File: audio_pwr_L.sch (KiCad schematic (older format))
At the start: 43 parts, among them Q201 BC546, Q202 BC546, Q203 BC546, Q204 BD140, Q205 BD139, Q206 BD140, Q207 MJL21193, Q208 MJL21194, Q209 BC546

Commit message: Lots of part changes to SMD devices. Adding MPN, MFG to all parts for BOM export.
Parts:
- removed F201, F202: 3A, Fuseholders:Fuseholder5x20_horiz_open_inline_Type-I, symbol Device:Fuse
- removed Q201, Q202: BC546, Package_TO_SOT_THT:TO-92_Inline, symbol AAMB-rescue:BC546-transistors
- added F201, F202: 0154003.DR, Fuse:0154003.DR, symbol Fuse:0154003.DR
- added TP7: 5002, digikey-footprints:Test_Point_D1.02mm, symbol dk_Test-Points:5002
- added TP8: 5000, digikey-footprints:Test_Point_D1.02mm, symbol dk_Test-Points:5000
- added TP9: 5001, digikey-footprints:Test_Point_D1.02mm, symbol dk_Test-Points:5001
- added U201: BC846BDW1T1G, Package_TO_SOT_SMD:SOT-363_SC-70-6, symbol OnSemi_BC846:BC846BDW1T1G
- C201: footprint Capacitor_THT:CP_Radial_D5.0mm_P2.00mm -> Capacitor_SMD:CP_Elec_4x5.4; DigiKey (none) -> https://www.we-online.de/katalog/datasheet/865080640004.pdf; MFG (none) -> Würth Elektronik; MPN (none) -> 865080640004
- C202, C204, C206: footprint Capacitor_THT:C_Disc_D5.1mm_W3.2mm_P5.00mm -> Capacitor_SMD:C_0603_1608Metric_Pad1.05x0.95mm_HandSolder; DigiKey (none) -> https://www.digikey.com/product-detail/en/w%C3%BCrth-elektr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; MFG (none) -> Würth Elektronik; MPN (none) -> 885012006057
- C203: footprint Capacitor_THT:CP_Radial_D10.0mm_P5.00mm -> Capacitor_SMD:C_Elec_5x5.4; DigiKey (none) -> https://www.digikey.com/product-detail/en/w%C3%BCrth-elektr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; MFG (none) -> Würth Elektronik; MPN (none) -> 865080142007
- C205: footprint Capacitor_THT:CP_Radial_D10.0mm_P5.00mm -> Capacitor_SMD:C_Elec_6.3x7.7; DigiKey (none) -> https://www.digikey.com/product-detail/en/w%C3%BCrth-elektr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; MFG (none) -> Würth Elektronik; MPN (none) -> 865080545012
- C207, C208, C209: DigiKey (none) -> https://www.digikey.com/product-detail/en/kemet/R82EC3100AA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; MFG (none) -> KEMET; MPN (none) -> R82EC3100AA70K
- C210, C211: footprint Capacitor_THT:CP_Radial_D10.0mm_P5.00mm -> Capacitor_SMD:CP_Elec_10x10.5; DigiKey (none) -> https://www.digikey.com/product-detail/en/nichicon/UUX1J101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; MFG (none) -> Nichicon; MPN (none) -> UUX1J101MNL1GS
- D201: footprint LED_THT:LED_D3.0mm -> LED_SMD:LED_0603_1608Metric_Pad1.05x0.95mm_HandSolder; DigiKey (none) -> https://www.digikey.com/product-detail/en/rohm-semiconducto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; MFG (none) -> Rohm Semiconductor; MPN (none) -> SML-D12U1WT86
- Q203, Q209: value BC546 -> BC846; footprint Package_TO_SOT_THT:TO-92_Inline -> Package_TO_SOT_SMD:SOT-23; DigiKey (none) -> https://www.digikey.com/product-detail/en/on-semiconductor/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; MFG (none) -> ON Semiconductor; MPN (none) -> BC846BLT1G
- Q204, Q206: value BD140 -> BCP53; footprint Package_TO_SOT_THT:TO-126-3_Vertical -> Package_TO_SOT_SMD:SOT-223; DigiKey (none) -> https://www.digikey.com/product-detail/en/on-semiconductor/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; MFG (none) -> ON Semiconductor; MPN (none) -> SBCP53-10T1G
- Q205: value BD139 -> BCP56; footprint Package_TO_SOT_THT:TO-126-3_Vertical -> Package_TO_SOT_SMD:SOT-223; DigiKey (none) -> https://www.digikey.com/product-detail/en/on-semiconductor/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; MFG (none) -> ON Semiconductor; MPN (none) -> SBCP56-16T3G
- R213, R214: value 15m -> 330m; footprint Resistor_THT:R_Axial_Power_L25.0mm_W9.0mm_P10.16mm_Vertical -> Resistor_THT:R_Radial_Power_L13.0mm_W9.0mm_P5.00mm; DigiKey (none) -> https://www.digikey.com/product-detail/en/te-connectivity-p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; MFG (none) -> TE Connectivity Passive Product; MPN (none) -> SQMW5R33J
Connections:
- wire segments 123 -> 128

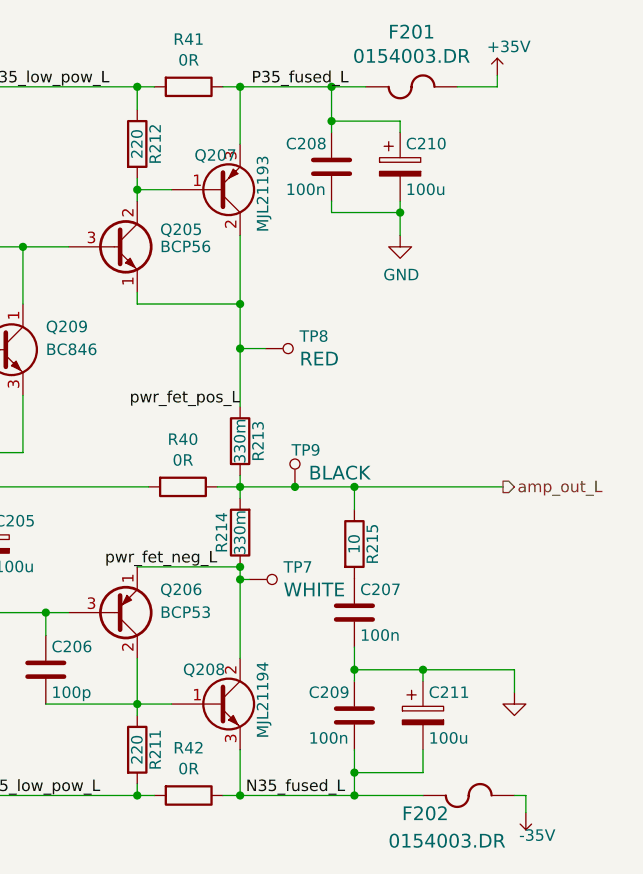
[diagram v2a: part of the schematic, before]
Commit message: Layout startover, sorting, some routing. Removed redundant fuses. BOM export.
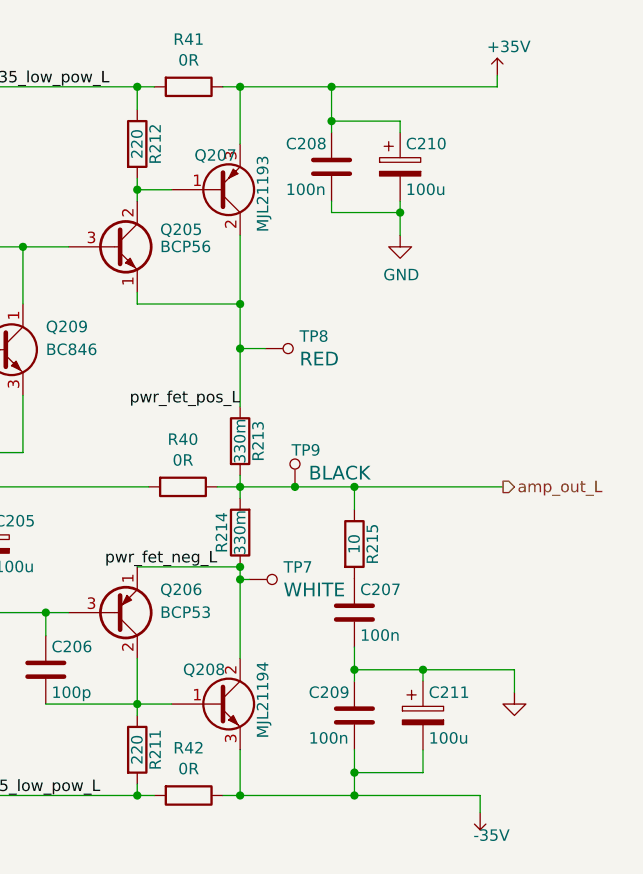
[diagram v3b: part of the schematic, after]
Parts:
- removed F201, F202: 0154003.DR, Fuse:0154003.DR, symbol Fuse:0154003.DR
- C201, C202, C203, C204, C205, C206: MFG Würth Elektronik -> Wurth Elektronik
- Q207: DigiKey (none) -> https://www.digikey.com/products/en/discrete-semiconductor-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; MFG (none) -> ON Semiconductor; MPN (none) -> MJL21193G
- Q208: DigiKey (none) -> https://www.digikey.com/products/en/discrete-semiconductor-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; MFG (none) -> ON Semiconductor; MPN (none) -> MJL21194G
- R201, R203, R204, R216: DigiKey (none) -> https://www.digikey.com/product-detail/en/vishay-dale/RCS06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; MFG (none) -> Vishay Dale; MPN (none) -> RCS06031K00FKEA
- R202, R205, R208: DigiKey (none) -> https://www.digikey.com/product-detail/en/te-connectivity-p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; MFG (none) -> TE Connectivity Passive Product; MPN (none) -> CRGCQ0603F22K
- R206, R207: DigiKey (none) -> https://www.digikey.com/product-detail/en/te-connectivity-p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; MFG (none) -> TE Connectivity Passive Product; MPN (none) -> CRGCQ0603F560R
- R209, R210: DigiKey (none) -> https://www.digikey.com/product-detail/en/vishay-dale/CRCW0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; MFG (none) -> Vishay Dale; MPN (none) -> CRCW06033K30FKEA
- R211, R212: DigiKey (none) -> https://www.digikey.com/product-detail/en/panasonic-electro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; MFG (none) -> Panasonic Electronic Components; MPN (none) -> ERJ-PA3F2200V
- R215: DigiKey (none) -> https://www.digikey.com/product-detail/en/panasonic-electro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; MFG (none) -> Panasonic Electronic Components; MPN (none) -> ERJ-PA3F10R0V
- R40, R41, R42: MFG (none) -> Stackpole Electronics Inc; MPN (none) -> RMCF1210ZT0R00
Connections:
- net N35_fused_L is gone; now on net -35V: C209.2, C211.2, Q208.3 (E), R42.1
- net P35_fused_L is gone; now on net +35V: C208.1, C210.1, Q207.3 (E), R41.1

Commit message: Capturing layout progress.
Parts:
- removed C201: 4.7u, Capacitor_SMD:CP_Elec_4x5.4, symbol Device:CP
- removed TP7: 5002, digikey-footprints:Test_Point_D1.02mm, symbol dk_Test-Points:5002
- removed TP8: 5000, digikey-footprints:Test_Point_D1.02mm, symbol dk_Test-Points:5000
- removed TP9: 5001, digikey-footprints:Test_Point_D1.02mm, symbol dk_Test-Points:5001
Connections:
- net amp_in_L: now also R201.2
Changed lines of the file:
@@
 Connection ~ 3300 4350
-Wire Wire Line
-	2900 3650 2950 3650
 Wire Wire Line
 	3850 4450 3850 4350
@@
 	6900 3600 6900 3650
 Connection ~ 6900 3650
-Wire Wire Line
-	6900 4000 6900 4055
 $Comp
 L Device:Q_PNP_BCE Q207
@@
 Wire Wire Line
 	6450 2350 6450 2400
-Wire Wire Line
-	6900 2850 6900 3045
 Connection ~ 3300 3800
 Text Label 6800 4000 2    50   ~ 0
@@
 Wire Wire Line
 	4900 4400 4900 4500
-Text HLabel 2450 3650 0    50   Input ~ 0
+Text HLabel 2700 3650 0    50   Input ~ 0
 amp_in_L
 Text HLabel 8050 3650 2    50   Output ~ 0
@@
 Wire Wire Line
 	7400 3650 8050 3650
-$Comp
-L Device:CP C201
-U 1 1 5C7F66CB
-P 2750 3650
-F 0 "C201" H 2775 3750 50  0000 L CNN
-F 1 "4.7u" H 2775 3550 50  0000 L CNN
-F 2 "Capacitor_SMD:CP_Elec_4x5.4" H 2788 3500 50  0001 C CNN
-F 3 "https://www.digikey.com/product-detail/en/w%C3%BCrth-elektronik/865080640004/732-8449-1-ND/5728406" H 2750 3650 50  0001 C CNN
-F 4 "https://www.we-online.de/katalog/datasheet/865080640004.pdf" H 2750 3650 50  0001 C CNN "DigiKey"
-F 5 "Wurth Elektronik" H 2750 3650 50  0001 C CNN "MFG"
-F 6 "865080640004" H 2750 3650 50  0001 C CNN "MPN"
-	1    2750 3650
-	0    -1   -1   0
-$EndComp
 $Comp
 L Device:R R203
@@
 	3000 4500 3000 4350
 Wire Wire Line
-	2450 3650 2600 3650
-Wire Wire Line
 	7600 2450 7600 2550
 $Comp
@@
 	7400 5000 6900 5000
 Connection ~ 7400 5000
-Wire Wire Line
-	7400 3650 7140 3650
 Connection ~ 7400 3650
 $Comp
@@
 Wire Wire Line
 	4700 3650 4900 3650
-$Comp
-L dk_Test-Points:5000 TP8
-U 1 1 5EA50D7D
-P 7110 3045
-F 0 "TP8" V 7163 2995 50  0000 R CNN
-F 1 "5000" H 7110 2945 50  0001 C CNN
-F 2 "digikey-footprints:Test_Point_D1.02mm" H 7310 3245 60  0001 L CNN
-F 3 "http://www.keyelco.com/product-pdf.cfm?p=1309" H 7310 3345 60  0001 L CNN
-F 4 "36-5000-ND" H 7310 3445 60  0001 L CNN "Digi-Key_PN"
-F 5 "5000" H 7310 3545 60  0001 L CNN "MPN"
-F 6 "Test and Measurement" H 7310 3645 60  0001 L CNN "Category"
-F 7 "Test Points" H 7310 3745 60  0001 L CNN "Family"
-F 8 "http://www.keyelco.com/product-pdf.cfm?p=1309" H 7310 3845 60  0001 L CNN "DK_Datasheet_Link"
-F 9 "/product-detail/en/keystone-electronics/5000/36-5000-ND/255326" H 7310 3945 60  0001 L CNN "DK_Detail_Page"
-F 10 "RED" V 7064 2995 60  0000 R CNN "Description"
-F 11 "Keystone Electronics" H 7310 4145 60  0001 L CNN "Manufacturer"
-F 12 "Active" H 7310 4245 60  0001 L CNN "Status"
-F 13 "/product-detail/en/keystone-electronics/5000/36-5000-ND/255326" H 7110 3045 50  0001 C CNN "DigiKey"
-F 14 "Keystone Electronics" H 7110 3045 50  0001 C CNN "MFG"
-	1    7110 3045
-	0    -1   -1   0
-$EndComp
-$Comp
-L dk_Test-Points:5001 TP9
-U 1 1 5EA52462
-P 7140 3550
-F 0 "TP9" H 7155 3490 50  0000 R CNN
-F 1 "5001" H 7140 3450 50  0001 C CNN
-F 2 "digikey-footprints:Test_Point_D1.02mm" H 7340 3750 60  0001 L CNN
-F 3 "http://www.keyelco.com/product-pdf.cfm?p=1310" H 7340 3850 60  0001 L CNN
-F 4 "36-5001-ND" H 7340 3950 60  0001 L CNN "Digi-Key_PN"
-F 5 "5001" H 7340 4050 60  0001 L CNN "MPN"
-F 6 "Test and Measurement" H 7340 4150 60  0001 L CNN "Category"
-F 7 "Test Points" H 7340 4250 60  0001 L CNN "Family"
-F 8 "http://www.keyelco.com/product-pdf.cfm?p=1310" H 7340 4350 60  0001 L CNN "DK_Datasheet_Link"
-F 9 "/product-detail/en/keystone-electronics/5001/36-5001-ND/255327" H 7340 4450 60  0001 L CNN "DK_Detail_Page"
-F 10 "BLACK" H 7080 3590 60  0000 R CNN "Description"
-F 11 "Keystone Electronics" H 7340 4650 60  0001 L CNN "Manufacturer"
-F 12 "Active" H 7340 4750 60  0001 L CNN "Status"
-F 13 "/product-detail/en/keystone-electronics/5001/36-5001-ND/255327" H 7140 3550 50  0001 C CNN "DigiKey"
-F 14 "Keystone Electronics" H 7140 3550 50  0001 C CNN "MFG"
-	1    7140 3550
-	-1   0    0    1
-$EndComp
-$Comp
-L dk_Test-Points:5002 TP7
-U 1 1 5EA53283
-P 7040 4055
-F 0 "TP7" V 7093 4005 50  0000 R CNN
-F 1 "5002" H 7040 3955 50  0001 C CNN
-F 2 "digikey-footprints:Test_Point_D1.02mm" H 7240 4255 60  0001 L CNN
-F 3 "http://www.keyelco.com/product-pdf.cfm?p=1311" H 7240 4355 60  0001 L CNN
-F 4 "36-5002-ND" H 7240 4455 60  0001 L CNN "Digi-Key_PN"
-F 5 "5002" H 7240 4555 60  0001 L CNN "MPN"
-F 6 "Test and Measurement" H 7240 4655 60  0001 L CNN "Category"
-F 7 "Test Points" H 7240 4755 60  0001 L CNN "Family"
-F 8 "http://www.keyelco.com/product-pdf.cfm?p=1311" H 7240 4855 60  0001 L CNN "DK_Datasheet_Link"
-F 9 "/product-detail/en/keystone-electronics/5002/36-5002-ND/255328" H 7240 4955 60  0001 L CNN "DK_Detail_Page"
-F 10 "WHITE" V 6994 4005 60  0000 R CNN "Description"
-F 11 "Keystone Electronics" H 7240 5155 60  0001 L CNN "Manufacturer"
-F 12 "Active" H 7240 5255 60  0001 L CNN "Status"
-F 13 "/product-detail/en/keystone-electronics/5002/36-5002-ND/255328" H 7040 4055 50  0001 C CNN "DigiKey"
-F 14 "Keystone Electronics" H 7040 4055 50  0001 C CNN "MFG"
-	1    7040 4055
-	0    -1   -1   0
-$EndComp
-Connection ~ 7140 3650
-Wire Wire Line
-	7140 3650 6900 3650
-Connection ~ 6900 3045
-Wire Wire Line
-	6900 3045 6900 3300
-Wire Wire Line
-	6900 3045 7010 3045
-Wire Wire Line
-	6940 4055 6900 4055
-Connection ~ 6900 4055
-Wire Wire Line
-	6900 4055 6900 4400
 Wire Wire Line
 	7300 1900 8025 1900
 Wire Wire Line
 	7400 5000 7950 5000
+Wire Wire Line
+	6900 3650 7400 3650
+Wire Wire Line
+	6900 2850 6900 3300
+Wire Wire Line
+	6900 4000 6900 4400
+Wire Wire Line
+	2700 3650 2950 3650
 $EndSCHEMATC

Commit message: Place and route complete. Silkscreen cleanup needed.
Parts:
- VR201: footprint Murata-POT:PV36W202C01B00 -> Potentiometer_THT:Potentiometer_Bourns_3296W_Vertical; DigiKey (none) -> https://www.digikey.com/product-detail/en/bourns-inc/3296W-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; MFG (none) -> Bourns Inc.; MPN (none) -> 3296W-1-202LF
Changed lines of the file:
@@
 F 0 "VR201" H 5350 3250 50  0000 R CNN
 F 1 "2k" V 5450 3300 50  0000 R CNN
-F 2 "Murata-POT:PV36W202C01B00" H 5450 3250 50  0001 C CNN
-F 3 "~" H 5450 3250 50  0001 C CNN
+F 2 "Potentiometer_THT:Potentiometer_Bourns_3296W_Vertical" H 5450 3250 50  0001 C CNN
+F 3 "https://www.bourns.com/docs/Product-Datasheets/3296.pdf" H 5450 3250 50  0001 C CNN
+F 4 "https://www.digikey.com/product-detail/en/bourns-inc/3296W-1-202LF/3296W-202LF-ND/1088050" H 5450 3250 50  0001 C CNN "DigiKey"
+F 5 "Bourns Inc." H 5450 3250 50  0001 C CNN "MFG"
+F 6 "3296W-1-202LF" H 5450 3250 50  0001 C CNN "MPN"
 	1    5450 3250
 	1    0    0    -1

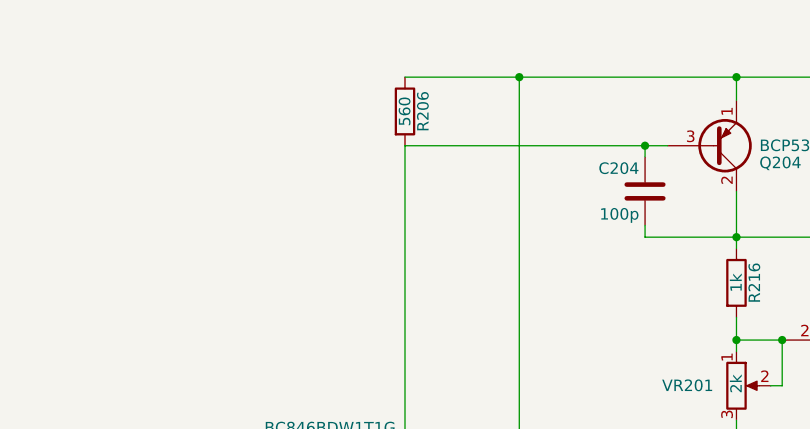
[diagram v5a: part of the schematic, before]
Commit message: Layout complete. Screw holes added and connected to GND.
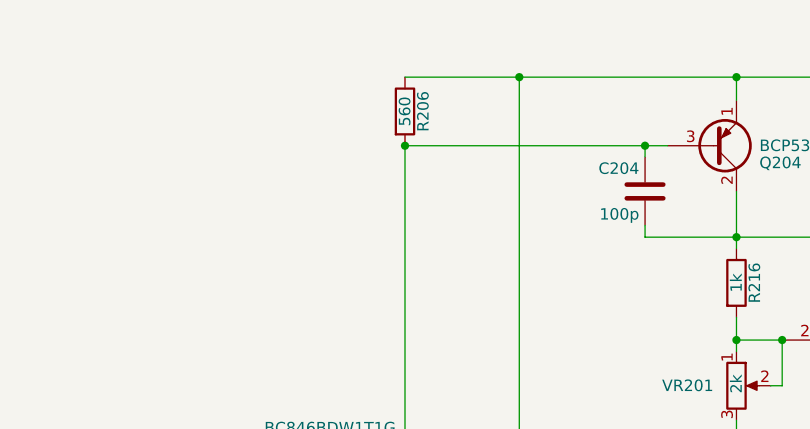
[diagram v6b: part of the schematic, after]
